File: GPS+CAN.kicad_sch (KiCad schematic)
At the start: 4 parts, among them U1 MCP25625x-x-ML, U6 TESEO-LIV4FTR

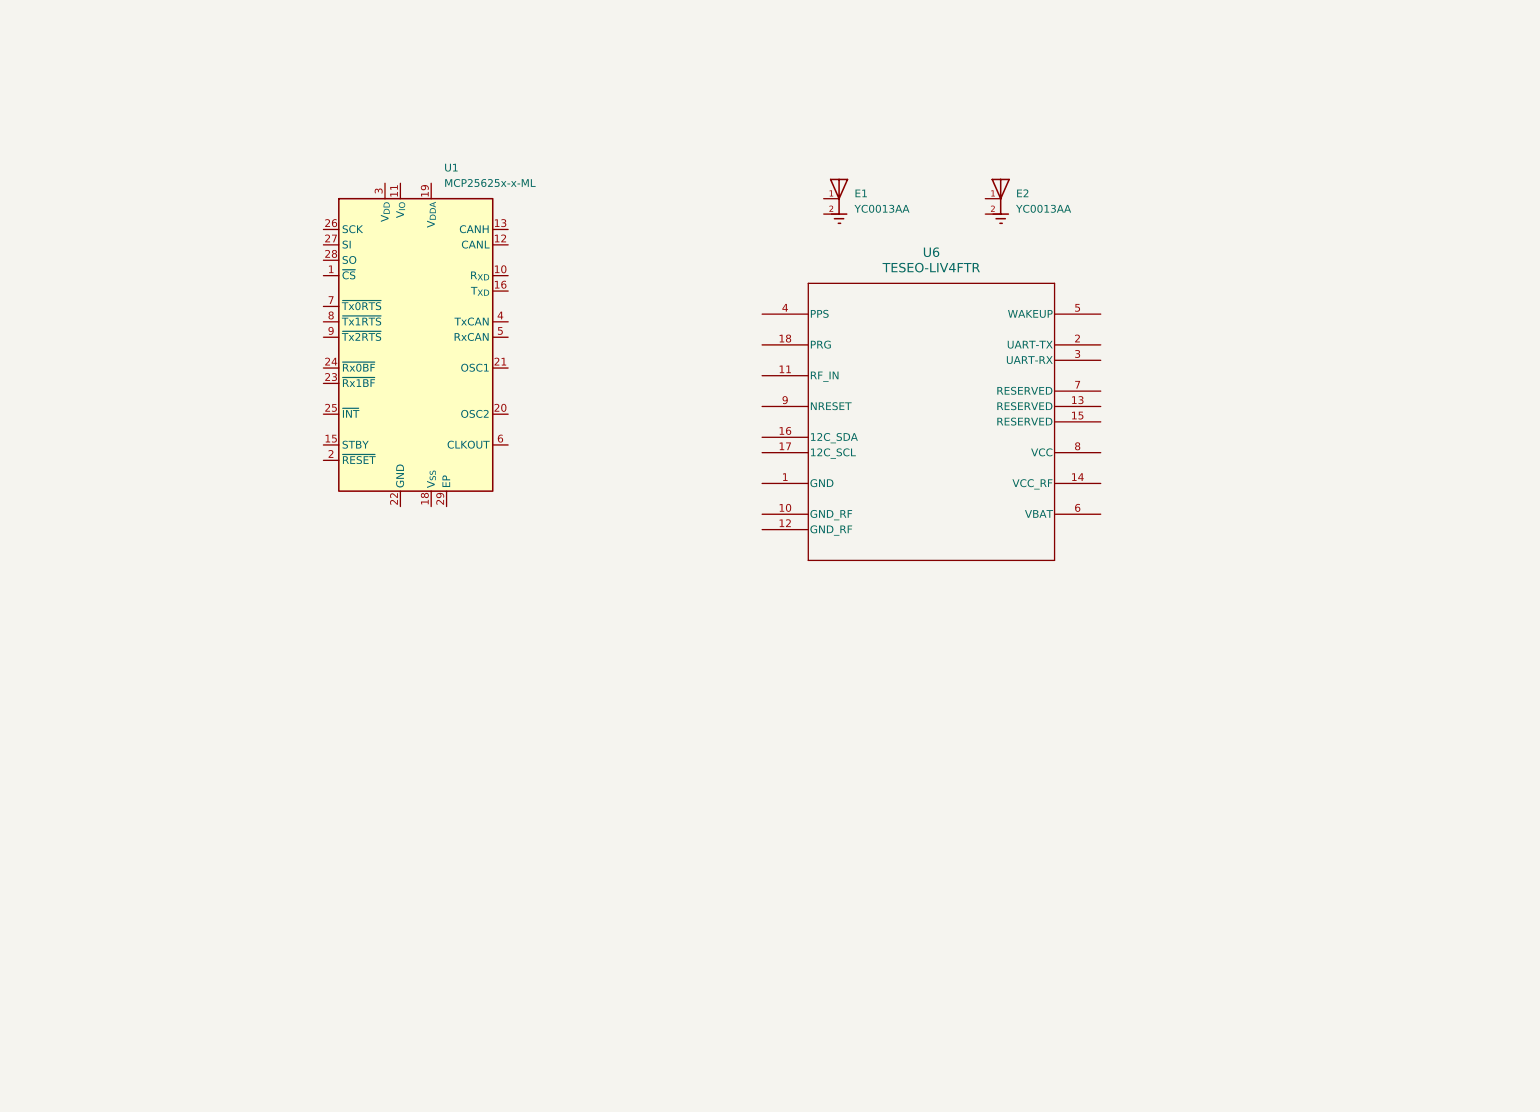
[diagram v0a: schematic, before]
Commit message: Fixed poorly uploaded symbols
Fixed poorly uploaded symbols but also added some components in the GPS+CAN subsheet.
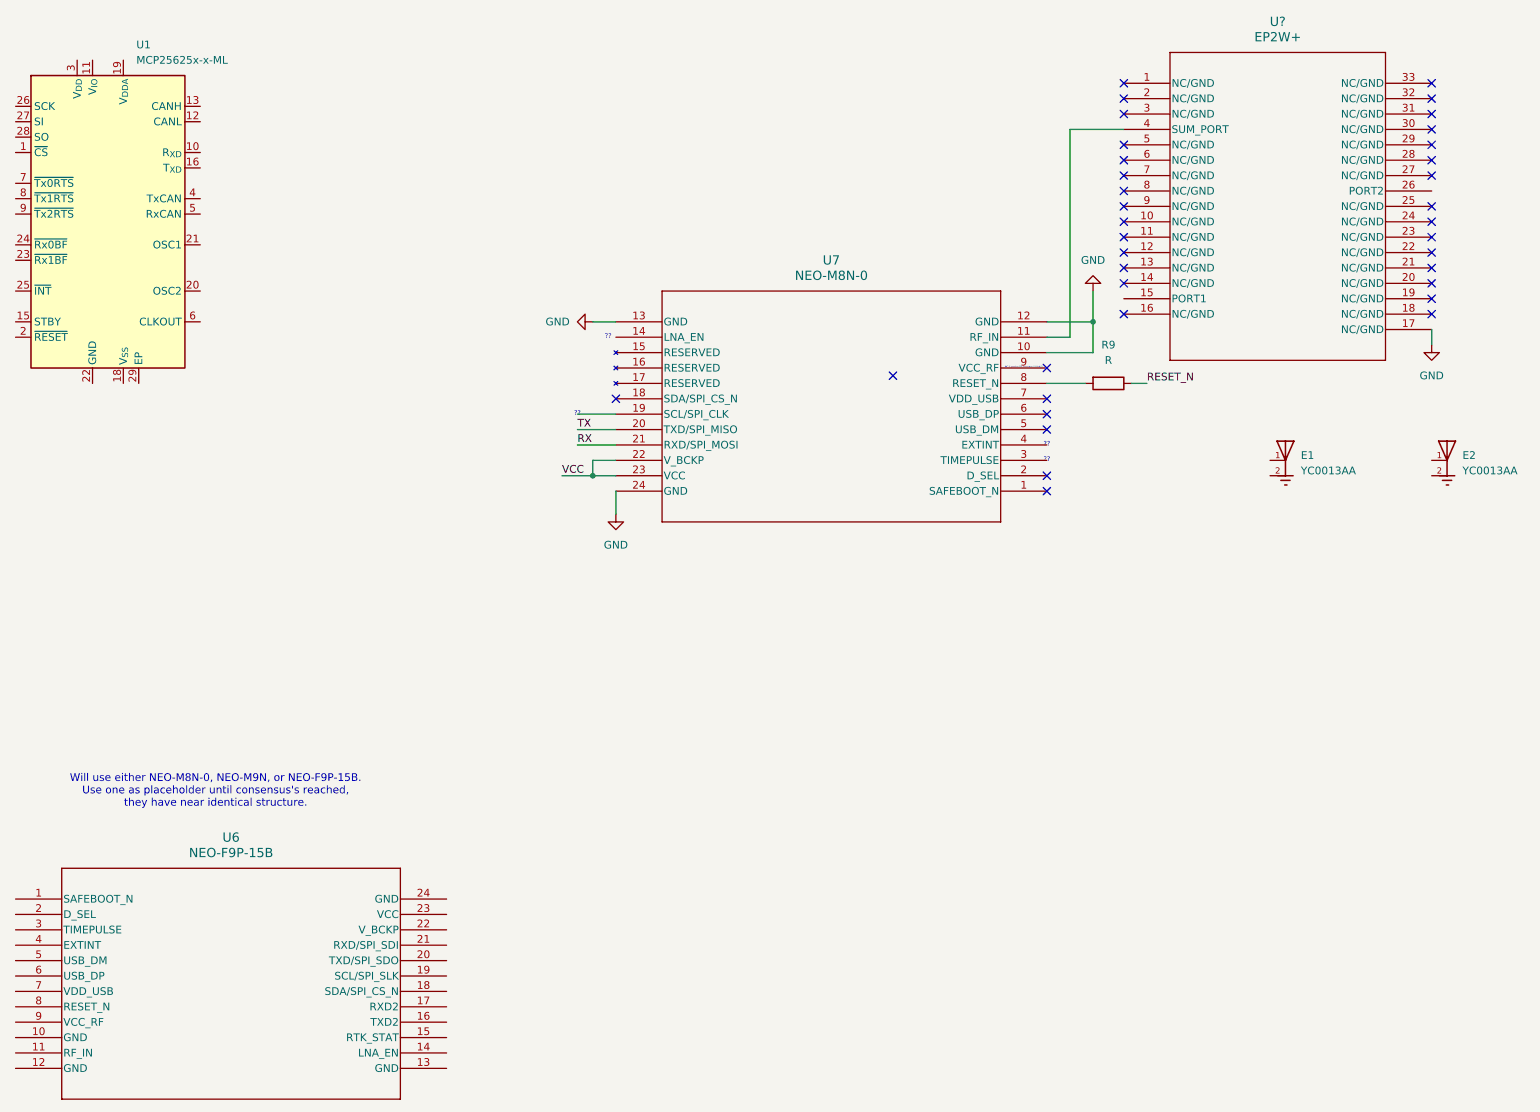
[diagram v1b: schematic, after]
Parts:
- removed U6: TESEO-LIV4FTR, LCC-18_STM, symbol 2026-06-19_06-08-10:TESEO-LIV4FTR
- added R9: R, symbol Device:R
- added U6: NEO-F9P-15B, MOD24_NEO-F9P-15B_UBL, symbol NEO-F9P-15B:NEO-F9P-15B
- added U7: NEO-M8N-0, MOD24_NEO-M8x_UBL, symbol NEO-M8N:NEO-M8N-0
- added U?: EP2W+, DG1677-2_MNC, symbol EP2W+:EP2W+
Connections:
- new net: U7.11 (RF_IN), U?.4 (SUM_PORT)
- new net: R9.2, U7.8 (RESET_N)
- new net GND: U7.10 (GND), U7.12 (GND), U7.13 (GND), U7.24 (GND), U?.17 (NC/GND)
- new net RESET_N: R9.1
- new net RX: U7.21 (RXD/SPI_MOSI)
- new net TX: U7.20 (TXD/SPI_MISO)
- new net VCC: U7.22 (V_BCKP), U7.23 (VCC)
- no-connect marks 0 -> 37
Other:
- note added: "??"
- note added: "NC if passive RF antennas (I think?)"
- note added: "Will use either NEO-M8N-0, NEO-M9N, or NEO-F9P-15B. Use one as placeholder until consensus's reached, they have near identical structure."
- moved on the sheet: E1, E2, U1
